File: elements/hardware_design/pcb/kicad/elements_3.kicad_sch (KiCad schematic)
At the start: 27 parts

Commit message: change LME49720 to tl072
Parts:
- IC14: value (none) -> TL072; footprint (none) -> elements:SO08
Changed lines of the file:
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@@
       (effects (font (size 1.778 1.5113)) (justify left bottom) hide)
     )
-    (property "Value" "" (id 1) (at 231.14 129.54 0)
+    (property "Value" "TL072" (id 1) (at 231.14 129.54 0)
       (effects (font (size 1.778 1.5113)) (justify left bottom) hide)
     )
-    (property "Footprint" "" (id 2) (at 228.6 134.62 0)
+    (property "Footprint" "elements:SO08" (id 2) (at 228.6 134.62 0)
       (effects (font (size 1.27 1.27)) hide)
     )
@@
       (effects (font (size 1.778 1.5113)) (justify left bottom) hide)
     )
-    (property "Value" "" (id 1) (at 309.88 157.48 0)
+    (property "Value" "TL072" (id 1) (at 309.88 157.48 0)
       (effects (font (size 1.778 1.5113)) (justify left bottom) hide)
     )
-    (property "Footprint" "" (id 2) (at 307.34 152.4 0)
+    (property "Footprint" "elements:SO08" (id 2) (at 307.34 152.4 0)
       (effects (font (size 1.27 1.27)) hide)
     )
@@
       (effects (font (size 1.778 1.5113)) (justify left bottom) hide)
     )
-    (property "Value" "" (id 1) (at 231.14 167.64 0)
+    (property "Value" "TL072" (id 1) (at 231.14 167.64 0)
       (effects (font (size 1.778 1.5113)) (justify left bottom) hide)
     )
-    (property "Footprint" "" (id 2) (at 228.6 172.72 0)
-      (effects (font (size 1.27 1.27)) hide)
-    )
+    (property "Footprint" "elements:SO08" (id 2) (at 228.6 172.72 0)
+      (effects (font (size 1.27 1.27)) hide)
+    )

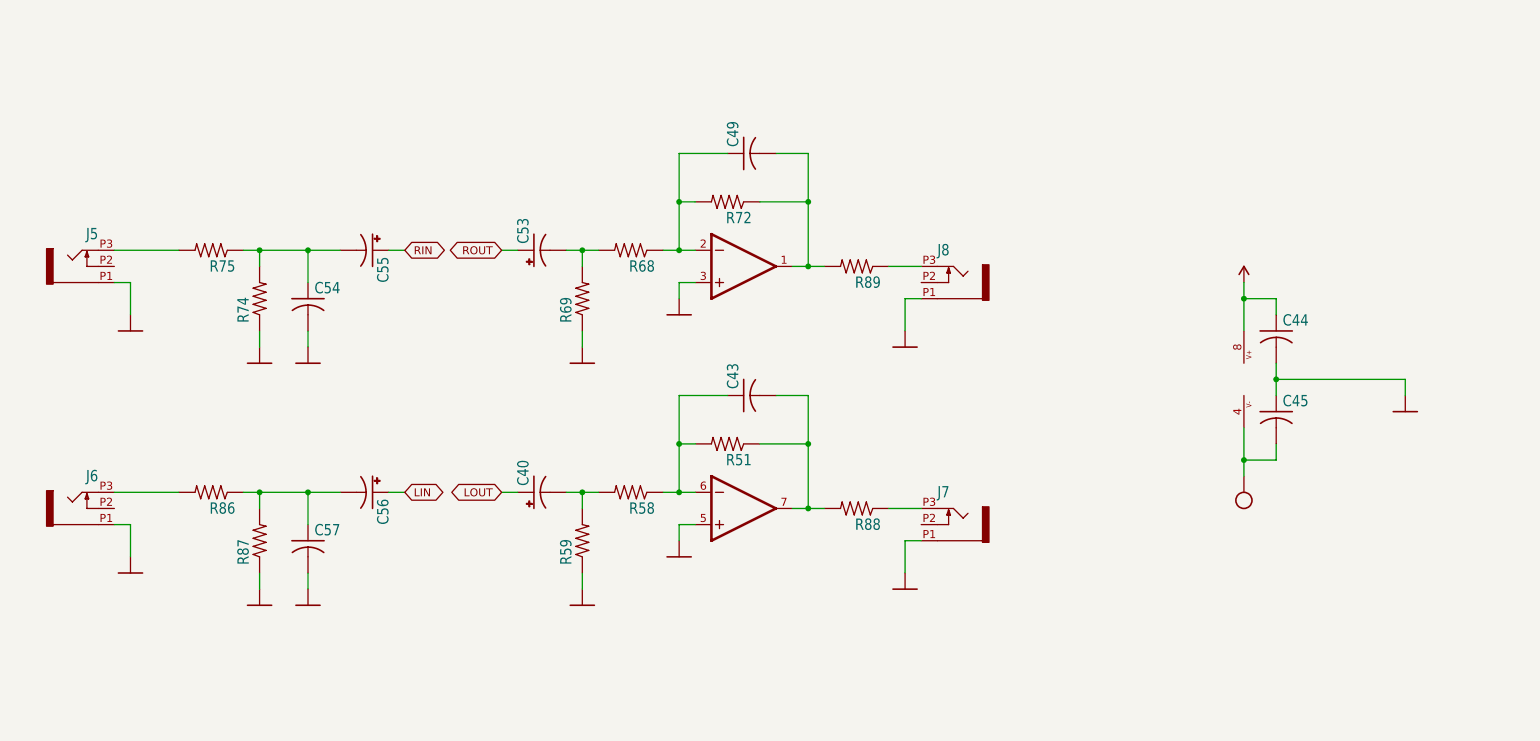
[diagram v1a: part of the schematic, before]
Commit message: swap wm8731 package (haven't drawn traces yet)
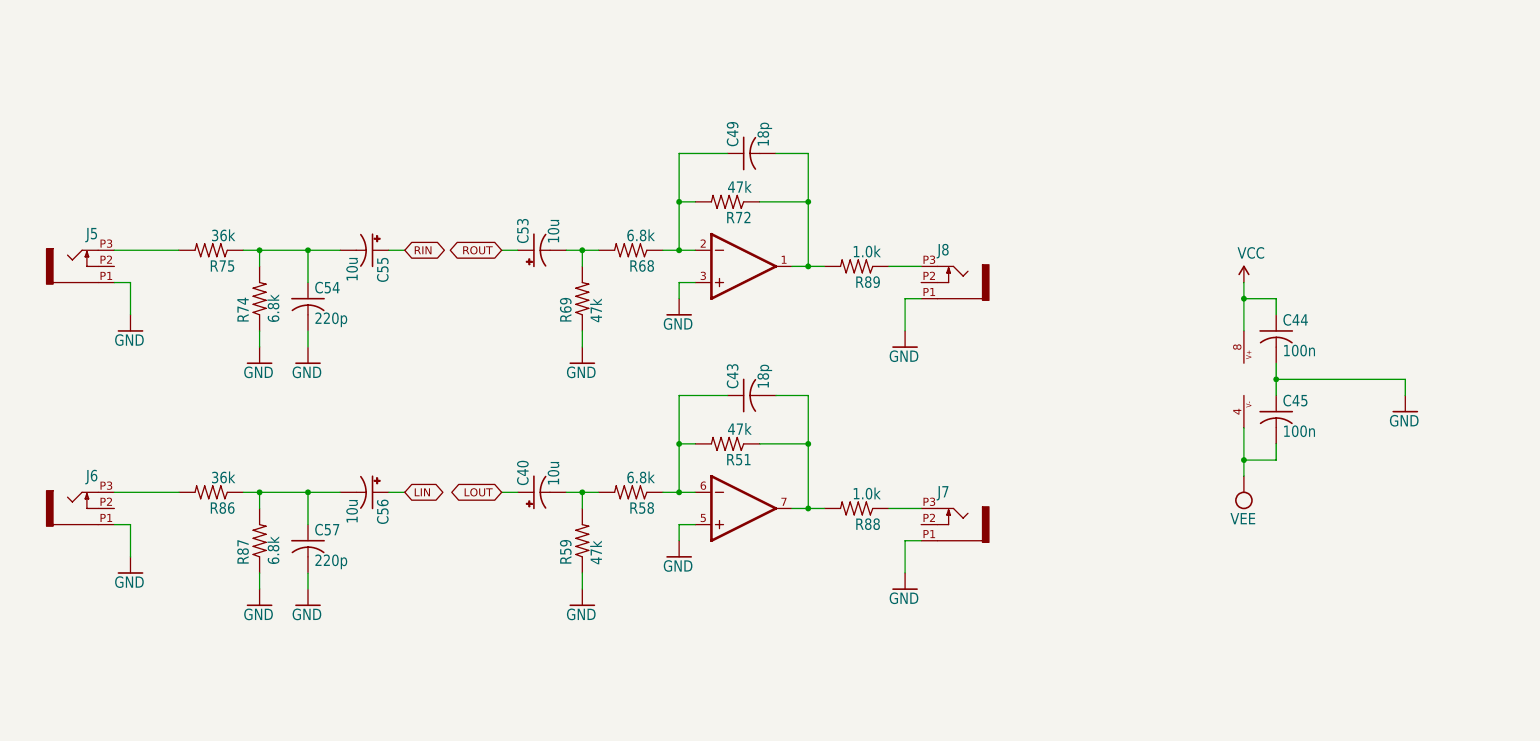
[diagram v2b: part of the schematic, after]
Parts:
- C40, C53, C55, C56: value (none) -> 10u; footprint (none) -> elements:PANASONIC_B
- C43, C49: value (none) -> 18p; footprint (none) -> elements:C0603
- C44, C45: value (none) -> 100n; footprint (none) -> elements:C0603
- C54, C57: value (none) -> 220p; footprint (none) -> elements:C0603
- J5, J6, J7, J8: value (none) -> PJ301_THONKICONN6; footprint (none) -> elements:WQP_PJ_301M6
- R51, R59, R69, R72: value (none) -> 47k; footprint (none) -> elements:R0603
- R58, R68, R74, R87: value (none) -> 6.8k; footprint (none) -> elements:R0603
- R75, R86: value (none) -> 36k; footprint (none) -> elements:R0603
- R88, R89: value (none) -> 1.0k; footprint (none) -> elements:R0603
